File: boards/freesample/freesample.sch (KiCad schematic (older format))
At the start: 20 parts, among them J1 SMA, J11 SMA, J12 SMA, J2 BARREL, M1 TRACEPAD, M2 LOGO1, M3 LOGO2, M4 LOGO3, M5 LOGO4, M6 LOGO5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

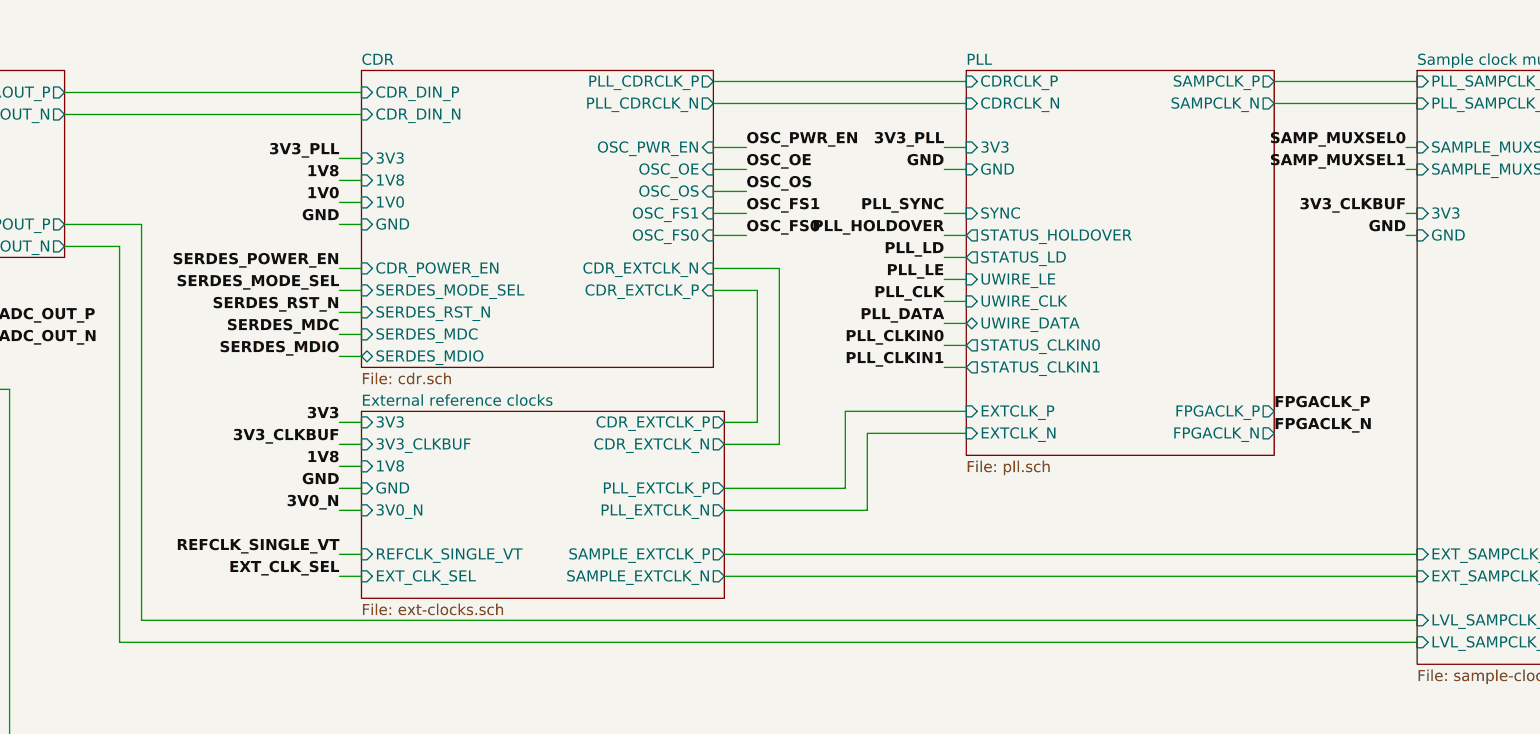
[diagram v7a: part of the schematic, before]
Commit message: Began layout on clock recovery block
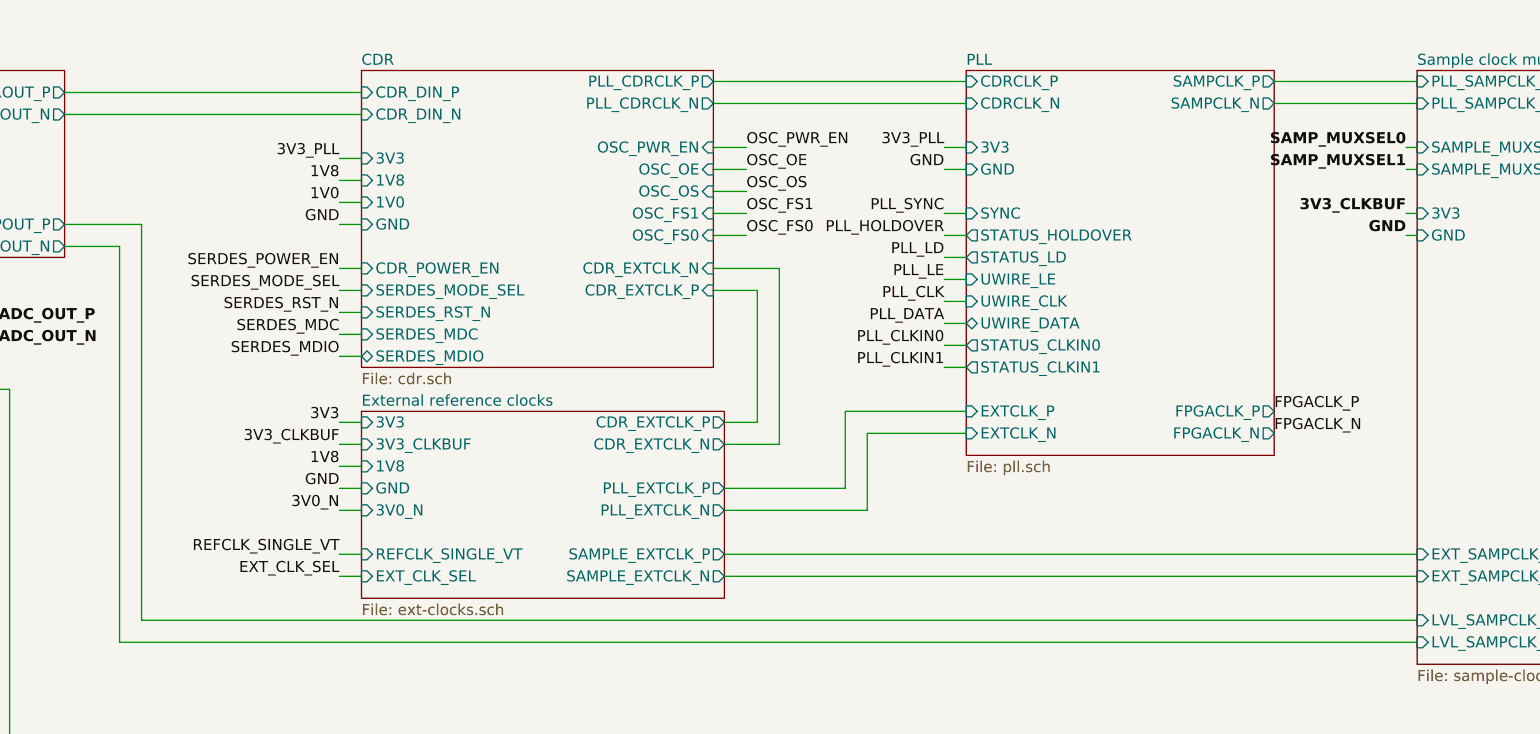
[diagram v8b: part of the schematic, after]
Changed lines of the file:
@@
 F12 "3V3_CLKBUF" I L 2750 1150 50
 $EndSheet
-Text Label 5550 1250 2    50   ~ 10
+Text Label 5550 1250 2    50   ~ 0
 1V8
 Wire Wire Line
 	5550 1250 5650 1250
-Text Label 5550 1350 2    50   ~ 10
+Text Label 5550 1350 2    50   ~ 0
 1V0
 Wire Wire Line
 	5550 1350 5650 1350
-Text Label 5550 1450 2    50   ~ 10
+Text Label 5550 1450 2    50   ~ 0
 GND
 Wire Wire Line
@@
 F15 "D3V3" I L 850 2100 50
 $EndSheet
-Text Label 8300 1100 2    50   ~ 10
+Text Label 8300 1100 2    50   ~ 0
 3V3_PLL
 Wire Wire Line
 	8300 1100 8400 1100
-Text Label 8300 1200 2    50   ~ 10
+Text Label 8300 1200 2    50   ~ 0
 GND
 Wire Wire Line
@@
 Wire Wire Line
 	750  3900 850  3900
-Text Label 5550 2350 2    50   ~ 10
+Text Label 5550 2350 2    50   ~ 0
 3V3
 Wire Wire Line
 	5650 2350 5550 2350
-Text Label 5550 2550 2    50   ~ 10
+Text Label 5550 2550 2    50   ~ 0
 1V8
 Wire Wire Line
 	5550 2550 5650 2550
-Text Label 5550 2650 2    50   ~ 10
+Text Label 5550 2650 2    50   ~ 0
 GND
 Wire Wire Line
 	5550 2650 5650 2650
-Text Label 5550 2750 2    50   ~ 10
+Text Label 5550 2750 2    50   ~ 0
 3V0_N
 Wire Wire Line
 	5550 2750 5650 2750
-Text Label 5550 2950 2    50   ~ 10
+Text Label 5550 2950 2    50   ~ 0
 REFCLK_SINGLE_VT
 Wire Wire Line
 	5550 2950 5650 2950
-Text Label 5550 3050 2    50   ~ 10
+Text Label 5550 3050 2    50   ~ 0
 EXT_CLK_SEL
 Wire Wire Line
@@
 Wire Wire Line
 	2100 4500 1950 4500
-Text Label 5550 1750 2    50   ~ 10
+Text Label 5550 1750 2    50   ~ 0
 SERDES_MODE_SEL
 Wire Wire Line
 	5550 1750 5650 1750
-Text Label 5550 1850 2    50   ~ 10
+Text Label 5550 1850 2    50   ~ 0
 SERDES_RST_N
 Wire Wire Line
 	5550 1850 5650 1850
-Text Label 5550 1950 2    50   ~ 10
+Text Label 5550 1950 2    50   ~ 0
 SERDES_MDC
 Wire Wire Line
 	5550 1950 5650 1950
-Text Label 5550 2050 2    50   ~ 10
+Text Label 5550 2050 2    50   ~ 0
 SERDES_MDIO
 Wire Wire Line
@@
 Text Label 1950 10350 0    50   ~ 10
 SERDES_MDIO
-Text Label 7400 1100 0    50   ~ 10
+Text Label 7400 1100 0    50   ~ 0
 OSC_PWR_EN
-Text Label 7400 1300 0    50   ~ 10
+Text Label 7400 1300 0    50   ~ 0
 OSC_OS
-Text Label 7400 1400 0    50   ~ 10
+Text Label 7400 1400 0    50   ~ 0
 OSC_FS1
-Text Label 7400 1500 0    50   ~ 10
+Text Label 7400 1500 0    50   ~ 0
 OSC_FS0
 Text Label 1950 7100 0    50   ~ 10
@@
 Text Label 1950 5500 0    50   ~ 10
 OSC_FS0
-Text Label 7400 1200 0    50   ~ 10
+Text Label 7400 1200 0    50   ~ 0
 OSC_OE
-Text Label 5550 1150 2    50   ~ 10
+Text Label 5550 1150 2    50   ~ 0
 3V3_PLL
 Wire Wire Line
@@
 Wire Wire Line
 	7250 800  8400 800
-Text Label 8300 1400 2    50   ~ 10
+Text Label 8300 1400 2    50   ~ 0
 PLL_SYNC
-Text Label 8300 1500 2    50   ~ 10
+Text Label 8300 1500 2    50   ~ 0
 PLL_HOLDOVER
-Text Label 8300 1600 2    50   ~ 10
+Text Label 8300 1600 2    50   ~ 0
 PLL_LD
-Text Label 8300 1700 2    50   ~ 10
+Text Label 8300 1700 2    50   ~ 0
 PLL_LE
-Text Label 8300 1800 2    50   ~ 10
+Text Label 8300 1800 2    50   ~ 0
 PLL_CLK
-Text Label 8300 1900 2    50   ~ 10
+Text Label 8300 1900 2    50   ~ 0
 PLL_DATA
-Text Label 8300 2000 2    50   ~ 10
+Text Label 8300 2000 2    50   ~ 0
 PLL_CLKIN0
-Text Label 8300 2100 2    50   ~ 10
+Text Label 8300 2100 2    50   ~ 0
 PLL_CLKIN1
 Text Label 1950 5600 0    50   ~ 10
@@
 Wire Wire Line
 	1800 2400 1700 2400
-Text Label 5550 2450 2    50   ~ 10
+Text Label 5550 2450 2    50   ~ 0
 3V3_CLKBUF
 Wire Wire Line
@@
 Wire Wire Line
 	4650 1450 4650 3250
-Text Label 5550 1650 2    50   ~ 10
+Text Label 5550 1650 2    50   ~ 0
 SERDES_POWER_EN
 Wire Wire Line
@@
 Text Notes 600  1350 0    50   ~ 10
 MAX -2V to +2V INPUT
-Text Label 9800 2300 0    50   ~ 10
+Text Label 9800 2300 0    50   ~ 0
 FPGACLK_P
-Text Label 9800 2400 0    50   ~ 10
+Text Label 9800 2400 0    50   ~ 0
 FPGACLK_N
 Text Label 1950 7300 0    50   ~ 10
